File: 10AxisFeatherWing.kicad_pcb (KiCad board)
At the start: 2 copper layers, 50.8 x 22.9 mm, 28 parts, among them J1 feather long, J2 feather short, J3 feather long, J4 feather short, J5 INT, J6 NRESET, U1 BNO055, U2 BME280, Y1 32.768kHz

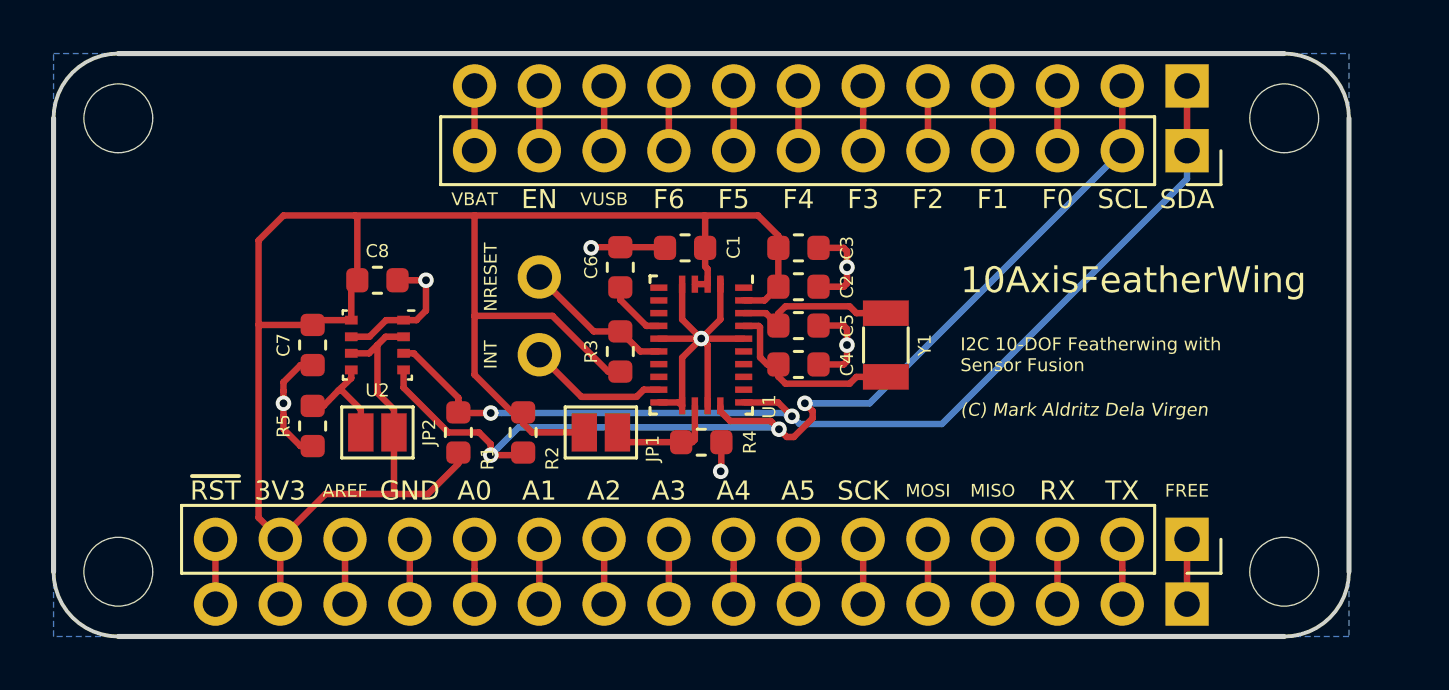
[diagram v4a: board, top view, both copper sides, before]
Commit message: Fixed electrical connections
Fixed the following electrical connection errors:
> Pin 6 on BNO055 not connected to GND
> SDA and SCL vias too close
> Pin 18 on BNO055 GND relocated
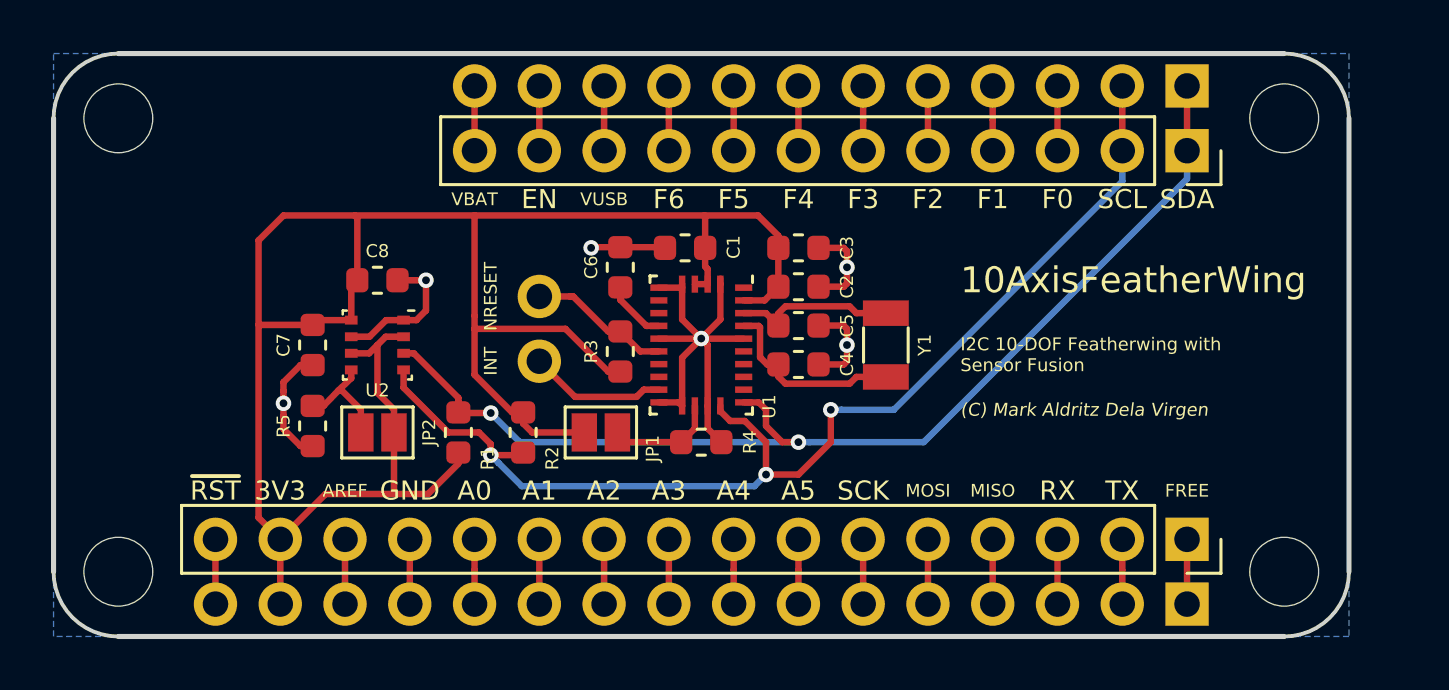
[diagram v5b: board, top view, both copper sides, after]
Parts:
- moved J6 0.76 mm to (44.5, 34.9)
- moved J5 0.25 mm to (44.5, 37.5)
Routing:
- net /SCL: track 42.9 -> 45.3 mm
- net /SDA: track 42.2 -> 43.8 mm
- net GND: track 39.3 -> 40.7 mm, vias 7 -> 6

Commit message: Fixed C7 not connected to BME280 pin 6
C7 is a decoupling capacitor, and should be connected to both VDD.
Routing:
- net +3V3: track 85.9 -> 82.9 mm
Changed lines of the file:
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@@
   (segment (start 51.05 39.2175) (end 51.05 40.1025) (width 0.254) (layer F.Cu) (net 13))
   (segment (start 36.83 44.45) (end 36.83 46.99) (width 0.254) (layer F.Cu) (net 14))
-  (segment (start 35.7475 35.855) (end 35.56 36.0425) (width 0.254) (layer F.Cu) (net 15))
-  (segment (start 37.075 35.855) (end 35.7475 35.855) (width 0.254) (layer F.Cu) (net 15))
   (segment (start 37.075 34.5275) (end 37.3125 34.29) (width 0.254) (layer F.Cu) (net 15))
   (segment (start 37.075 35.855) (end 37.075 34.5275) (width 0.254) (layer F.Cu) (net 15))
   (segment (start 37.075 37.155) (end 37.775 37.155) (width 0.254) (layer F.Cu) (net 15))
   (segment (start 38.425 36.505) (end 39.125 36.505) (width 0.254) (layer F.Cu) (net 15))
-  (segment (start 38.75 39.3566) (end 38.1 38.7066) (width 0.254) (layer F.Cu) (net 15))
-  (segment (start 38.75 40.259) (end 38.75 39.3566) (width 0.254) (layer F.Cu) (net 15))
   (segment (start 37.775 37.155) (end 38.1 36.83) (width 0.254) (layer F.Cu) (net 15))
-  (segment (start 38.1 38.7066) (end 38.1 36.83) (width 0.254) (layer F.Cu) (net 15))
   (segment (start 38.1 36.83) (end 38.425 36.505) (width 0.254) (layer F.Cu) (net 15))
   (segment (start 43.815 39.909) (end 43.815 39.4715) (width 0.254) (layer F.Cu) (net 15))
@@
   (segment (start 41.91 36.195) (end 41.91 35.687) (width 0.254) (layer F.Cu) (net 15))
   (segment (start 41.91 37.997382) (end 41.91 36.195) (width 0.254) (layer F.Cu) (net 15))
+  (segment (start 36.035 36.0425) (end 36.195 36.2025) (width 0.254) (layer F.Cu) (net 15))
+  (segment (start 35.56 36.0425) (end 36.035 36.0425) (width 0.254) (layer F.Cu) (net 15))
+  (segment (start 36.571 37.155) (end 37.075 37.155) (width 0.254) (layer F.Cu) (net 15))
+  (segment (start 36.195 36.779) (end 36.571 37.155) (width 0.254) (layer F.Cu) (net 15))
+  (segment (start 36.195 36.2025) (end 36.195 36.779) (width 0.254) (layer F.Cu) (net 15))
   (segment (start 31.75 44.45) (end 31.75 46.99) (width 0.254) (layer F.Cu) (net 16))
   (via (at 54.61 40.64) (size 0.6096) (drill 0.3048) (layers F.Cu B.Cu) (net 17))

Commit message: I2C pull-up resistor fix
Changed I2C pull-up resistor values from 10K to 4.7K
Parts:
- R1, R2: value 10K -> 4.7K
